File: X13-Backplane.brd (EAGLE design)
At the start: 101.6 x 139.3 mm, 57 parts, among them J1 284512-4, J11 284512-8, J12 284512-8, J2 284512-4, J3 284512-8, J4 284512-8, J5 284512-4, T1 284512-3, T2 284512-3, T3 284512-3, T4 284512-3, T5 284512-3, T6 284512-3, T7 284512-3, T8 284512-3, U1 ULN2003V12, Y1 ECS-80-S-4X

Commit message: draft board layout-  missing power connector
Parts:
- removed C1, C10, C2, C7, C8, C9: 4.7uF, SparkFun-Capacitors:0603
- removed C11: 0.1uF, SparkFun-Capacitors:0603
- removed C3, C4: 100nF, SparkFun-Capacitors:0603
- removed C5: 0.01uF, SparkFun-Capacitors:0603
- removed C6: 1uF, SparkFun-Capacitors:0603
- removed D1, D2, D4: (no value), SparkFun-LED:LED-0603
- removed J11, J12: 284512-8, 284512-8:TE_284512-8
- removed R10, R11: 1k, SparkFun-Resistors:0603
- removed R4, R6: 470, SparkFun-Resistors:0603
- removed R5: 22k, SparkFun-Resistors:0603
- removed R7: (no value), SparkFun-Resistors:0603
- removed R8: 10k, SparkFun-Resistors:0603
- removed R9: 4.7k, SparkFun-Resistors:0603
- removed RESET: (no value), DiscreteComponents:SW_2512
- removed SV1: (no value), con-lsta:FE05-1
- removed U$1, U$2, U$4, U$5, U$6: ESC2BACKPLANE, ESC_to_Backplane_Connectors:ESC2BACKPLANE_WHOLE
- removed U1: ULN2003V12, ULN2003V12:ULN2003V12
- removed Y1: ECS-80-S-4X, ECS-80-S-4X:XTAL_ECS-80-S-4X
- R1: value 1k -> 22k
- R2: value 1k -> 10k
- R3: value 1k -> 4.7k
- U$3: value STM32F042K6T6 -> ESC2BACKPLANE; device PI_Shield_Library:STM32F042K6T6 -> ESC_to_Backplane_Connectors:ESC2BACKPLANE_WHOLE
- U$8: value TCAN337D -> ESC2BACKPLANE; device PI_Shield_Library:TCAN337D -> ESC_to_Backplane_Connectors:ESC2BACKPLANE_WHOLE
- moved J1 329.9 mm to (6.35, 118.1), turned to 90 degrees
- moved T2 243.5 mm to (99.1, 6.35), flipped to the bottom, turned to 180 degrees
- moved T1 233.2 mm to (99.1, 17.8), flipped to the bottom, turned to 180 degrees
- moved MC4 223.3 mm to (99.1, 29.2), flipped to the bottom, turned to 180 degrees
- moved MC3 213.7 mm to (99.1, 40.6), flipped to the bottom, turned to 180 degrees
- moved MC2 204.5 mm to (99.1, 52.1), flipped to the bottom, turned to 180 degrees
- moved MC1 195.8 mm to (99.1, 63.5), flipped to the bottom, turned to 180 degrees
- moved U$7 163.9 mm to (33.0, 96.5), turned to 270 degrees
- moved R3 161.7 mm to (62.2, 36.8), turned to 90 degrees
- moved J4 157.5 mm to (96.5, 86.4), turned to 270 degrees
- moved MUX 149.9 mm to (85.1, 108.0)
- moved R2 139.6 mm to (62.2, 76.2), turned to 90 degrees
- moved J3 129.8 mm to (96.5, 121.9), turned to 270 degrees
- moved U$3 127.0 mm to (33.0, 135.9), turned to 270 degrees
- moved R1 126.4 mm to (62.2, 115.6), turned to 90 degrees
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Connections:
- removed net +3V3: C10.1, U$8.VCC
- removed net ALERT: U$3.PB7
- removed net CAN_RX: U$3.PA11, U$8.RXD
- removed net CAN_TX: U$3.PA12, U$8.TXD
- removed net CLK: U$3.PA9
- removed net DATA: U$3.PA10
- removed net GPIO0: U$3.PA2
- removed net GPIO1: U$3.PB6, U1.4
- removed net GPIO10: U$3.PA5, U1.3
- removed net GPIO11: U$3.PA6, U1.2
- removed net GPIO12: U$3.PA7, U1.1
- removed net GPIO13: U$3.PA8
- removed net GPIO14: U$3.PA1
- removed net GPIO15: U$3.PA0
- removed net GPIO2: U$3.PB4, U1.5
- removed net GPIO3: U$3.PB3, U1.6
- removed net GPIO8: U$3.PA3
- removed net GPIO9: U$3.PA4
- removed net LED: R7.2, U$3.PA15
- removed net N$1: C9.1, R1.1, Y1.2
- removed net N$2: C8.1, R3.1, Y1.1
- removed net N$24: D1.A, R7.1
- removed net N$25: D4.A, R4.1
- removed net N$27: D2.A, R6.1
- removed net N$3: R5.1
- removed net N$5: C11.2, R10.1, R11.2
- removed net OSC_IN: R3.2, U$3.PF0-OSC_IN
- removed net OSC_OUT: R1.2, U$3.PF1-OSC_OUT
- removed net SOL1_1: J12.1, U1.16
- removed net SOL2_1: J12.2, U1.15
- removed net SOL3_1: J12.3, U1.14
- removed net SOL4_1: J12.4, U1.13
- removed net SOL5_1: J12.5, U1.12
- removed net SOL6_1: J12.6, U1.11
- removed net SWCLK: SV1.4
- removed net SWDIO: SV1.2
- net 12V: now also U$3.P$10, U$3.P$11, U$3.P$12, U$3.P$13, U$3.P$9, U$3.P$A, U$3.P$B, U$3.P$C, U$3.P$D, U$3.P$E, U$3.P$O, U$3.P$P, U$3.P$Q, U$3.P$R, U$3.P$S, U$7.P$A, U$7.P$B, U$7.P$C, U$7.P$D, U$7.P$E, U$7.P$O, U$7.P$P, U$7.P$Q, U$7.P$R, U$7.P$S, U$8.P$10, U$8.P$11, U$8.P$12, U$8.P$13, U$8.P$9, U$8.P$A, U$8.P$B, U$8.P$C, U$8.P$D, U$8.P$E, U$8.P$O, U$8.P$P, U$8.P$Q, U$8.P$R, U$8.P$S; no longer J12.7, R4.2, U$1.P$A, U$1.P$B, U$1.P$C, U$1.P$D, U$1.P$E, U$1.P$O, U$1.P$P, U$1.P$Q, U$1.P$R, U$1.P$S, U$2.P$10, U$2.P$11, U$2.P$12, U$2.P$13, U$2.P$23, U$2.P$24, U$2.P$25, U$2.P$26, U$2.P$27, U$2.P$9, U$4.P$A, U$4.P$B, U$4.P$C, U$4.P$D, U$4.P$E, U$4.P$O, U$4.P$P, U$4.P$Q, U$4.P$R, U$4.P$S, U$5.P$10, U$5.P$11, U$5.P$12, U$5.P$13, U$5.P$23, U$5.P$24, U$5.P$25, U$5.P$26, U$5.P$27, U$5.P$9, U$6.P$A, U$6.P$B, U$6.P$C, U$6.P$D, U$6.P$E, U$6.P$O, U$6.P$P, U$6.P$Q, U$6.P$R, U$6.P$S, U$7.P$23, U$7.P$24, U$7.P$25, U$7.P$26, U$7.P$27, U1.9
- net 3.3V: now also U$3.P$G, U$3.P$H, U$3.P$U, U$3.P$V, U$7.P$G, U$7.P$H, U$7.P$U, U$7.P$V, U$8.P$G, U$8.P$H, U$8.P$U, U$8.P$V; no longer C1.1, C2.1, C3.1, C4.1, C5.1, C6.1, J11.5, R2.2, R6.2, SV1.5, U$1.P$G, U$1.P$H, U$1.P$U, U$1.P$V, U$3.VDD, U$3.VDDA, U$3.VDDIO2, U$4.P$G, U$4.P$H, U$4.P$U, U$4.P$V, U$6.P$G, U$6.P$H, U$6.P$U, U$6.P$V
- net CAN_H: now also U$3.P$6, U$8.P$6; no longer R10.2, U$2.P$6, U$5.P$6, U$8.CANH
- net CAN_L: now also U$3.P$7, U$8.P$7; no longer R11.1, U$2.P$7, U$5.P$7, U$8.CANL
- net ESC-ID_1: now also R1.2, U$3.P$8; no longer R5.2, U$7.P$8
- net ESC-ID_2: now also R2.2, U$7.P$8; no longer R8.2, U$5.P$8
- net ESC-ID_3: now also R3.2, U$8.P$8; no longer R9.2, U$2.P$8
- net GND: now also R1.1, R2.1, R3.1, U$3.P$1, U$3.P$15, U$3.P$16, U$3.P$17, U$3.P$18, U$3.P$2, U$3.P$23, U$3.P$24, U$3.P$25, U$3.P$26, U$3.P$27, U$3.P$3, U$3.P$4, U$3.P$AA, U$3.P$BB, U$3.P$J, U$3.P$K, U$3.P$L, U$3.P$M, U$3.P$N, U$3.P$X, U$3.P$Y, U$3.P$Z, U$7.P$23, U$7.P$24, U$7.P$25, U$7.P$26, U$7.P$27, U$7.P$AA, U$7.P$BB, U$7.P$J, U$7.P$K, U$7.P$L, U$7.P$M, U$7.P$N, U$7.P$X, U$7.P$Y, U$7.P$Z, U$8.P$1, U$8.P$15, U$8.P$16, U$8.P$17, U$8.P$18, U$8.P$2, U$8.P$23, U$8.P$24, U$8.P$25, U$8.P$26, U$8.P$27, U$8.P$3, U$8.P$4, U$8.P$AA, U$8.P$BB, U$8.P$J, U$8.P$K, U$8.P$L, U$8.P$M, U$8.P$N, U$8.P$X, U$8.P$Y, U$8.P$Z; no longer C1.2, C10.2, C11.1, C2.2, C3.2, C4.2, C5.2, C6.2, C7.2, C8.2, C9.2, D1.C, D2.C, D4.C, J11.1, R8.1, R9.1, RESET.1, SV1.3, U$1.P$AA, U$1.P$BB, U$1.P$J, U$1.P$K, U$1.P$L, U$1.P$M, U$1.P$N, U$1.P$X, U$1.P$Y, U$1.P$Z, U$2.P$1, U$2.P$15, U$2.P$16, U$2.P$17, U$2.P$18, U$2.P$2, U$2.P$3, U$2.P$4, U$3.PB8-BOOT0, U$3.VSS, U$3.VSS1, U$4.P$AA, U$4.P$BB, U$4.P$J, U$4.P$K, U$4.P$L, U$4.P$M, U$4.P$N, U$4.P$X, U$4.P$Y, U$4.P$Z, U$5.P$1, U$5.P$15, U$5.P$16, U$5.P$17, U$5.P$18, U$5.P$2, U$5.P$3, U$5.P$4, U$6.P$AA, U$6.P$BB, U$6.P$J, U$6.P$K, U$6.P$L, U$6.P$M, U$6.P$N, U$6.P$X, U$6.P$Y, U$6.P$Z, U$8.GND, U1.8
- net NRST: now also U$3.P$20, U$8.P$20; no longer C7.1, J11.6, R2.1, RESET.2, SV1.1, U$2.P$20, U$3.NRST, U$5.P$20
- net PROG_1: now also U$3.P$5; no longer J11.2, U$7.P$5
- net PROG_2: now also U$7.P$5; no longer J11.3, U$5.P$5
- net PROG_3: now also U$8.P$5; no longer J11.4, U$2.P$5
- net SWCLK_1: now also U$3.P$22; no longer U$7.P$22
- net SWCLK_2: now also U$7.P$22; no longer U$5.P$22
- net SWCLK_3: now also U$8.P$22; no longer U$2.P$22
- net SWCLK_4: no longer U$3.PA14
- net SWCLK_IN: no longer J11.7
- net SWDIO_1: now also U$3.P$21; no longer U$7.P$21
- net SWDIO_2: now also U$7.P$21; no longer U$5.P$21
- net SWDIO_3: now also U$8.P$21; no longer U$2.P$21
- net SWDIO_4: no longer U$3.PA13
- net SWDIO_IN: no longer J11.8, J12.8

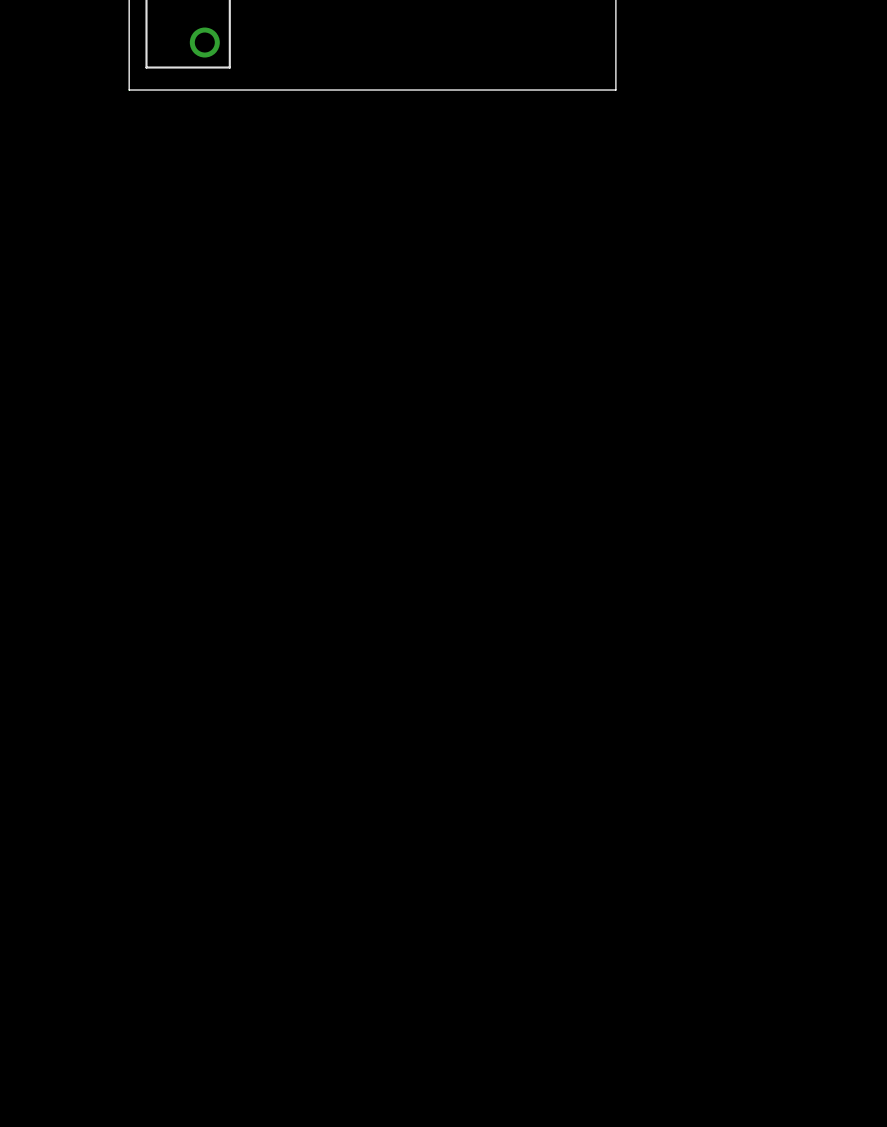
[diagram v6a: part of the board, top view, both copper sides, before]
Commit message: added back solenoid board
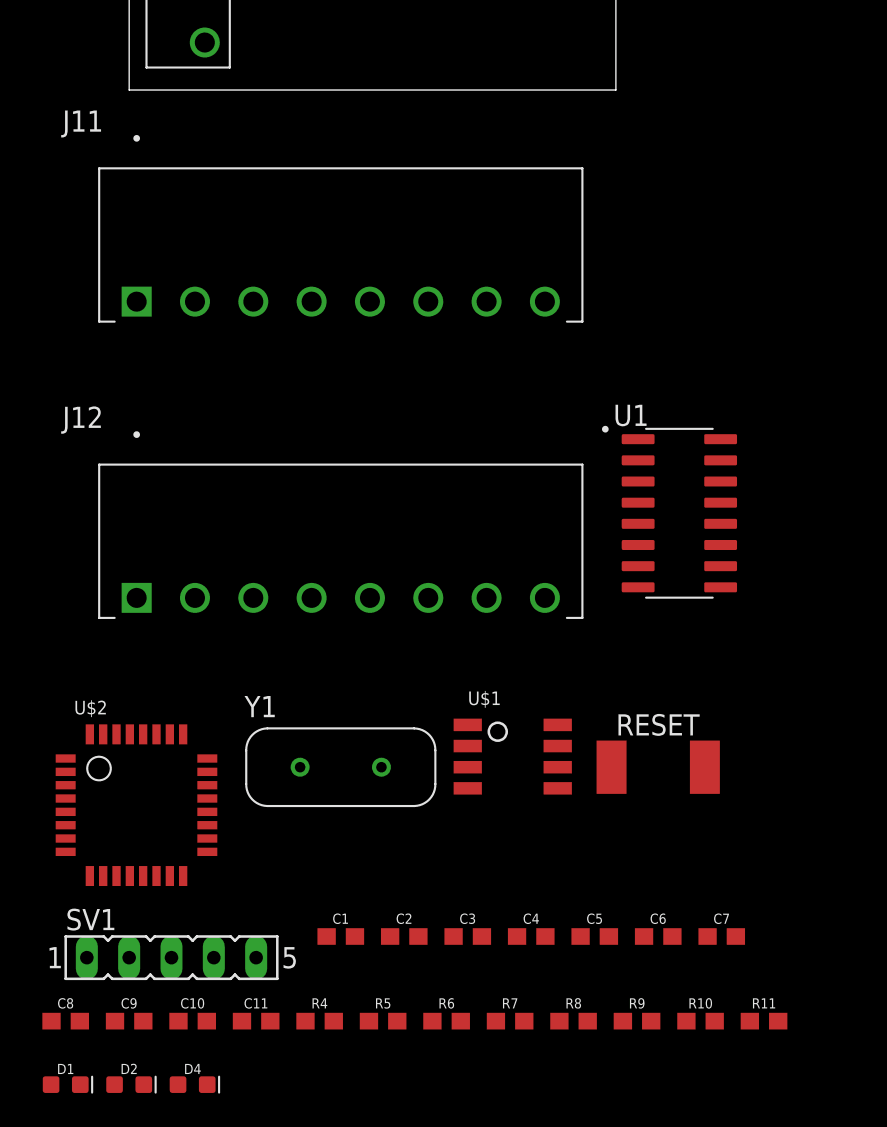
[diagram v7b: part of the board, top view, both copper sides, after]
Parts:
- added C1, C10, C2, C7, C8, C9: 4.7uF, SparkFun-Capacitors:0603
- added C11: 0.1uF, SparkFun-Capacitors:0603
- added C3, C4: 100nF, SparkFun-Capacitors:0603
- added C5: 0.01uF, SparkFun-Capacitors:0603
- added C6: 1uF, SparkFun-Capacitors:0603
- added D1, D2, D4: (no value), SparkFun-LED:LED-0603
- added J11, J12: 284512-8, 284512-8:TE_284512-8
- added R10, R11, R5, R7, R8: 1k, SparkFun-Resistors:0603
- added R4, R6: 470, SparkFun-Resistors:0603
- added R9: (no value), SparkFun-Resistors:0603
- added RESET: (no value), DiscreteComponents:SW_2512
- added SV1: (no value), con-lsta:FE05-1
- added U$1: TCAN337D, PI_Shield_Library:TCAN337D
- added U$2: STM32F042K6T6, PI_Shield_Library:STM32F042K6T6
- added U1: ULN2003V12, ULN2003V12:ULN2003V12
- added Y1: ECS-80-S-4X, ECS-80-S-4X:XTAL_ECS-80-S-4X
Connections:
- new net +3V3: C10.1, U$1.VCC
- new net ALERT1: U$2.PB7
- new net ALERT2: U$2.PB5
- new net C2_1: U$2.PB0
- new net C2_2: U$2.PB1
- new net CAN_RX: U$1.RXD, U$2.PA11
- new net CAN_TX: U$1.TXD, U$2.PA12
- new net CLK: U$2.PA9
- new net DATA: U$2.PA10
- new net GPIO0: U$2.PA2
- new net GPIO1: U$2.PB6, U1.4
- new net GPIO10: U$2.PA5, U1.3
- new net GPIO11: U$2.PA6, U1.2
- new net GPIO12: U$2.PA7, U1.1
- new net GPIO13: U$2.PA8
- new net GPIO14: U$2.PA1
- new net GPIO15: U$2.PA0
- new net GPIO2: U$2.PB4, U1.5
- new net GPIO3: U$2.PB3, U1.6
- new net GPIO8: U$2.PA3
- new net GPIO9: U$2.PA4
- new net LED: R9.2, U$2.PA15
- new net N$1: C9.1, R5.1, Y1.2
- new net N$2: C8.1, R8.1, Y1.1
- new net N$24: D1.A, R9.1
- new net N$25: D4.A, R4.1
- new net N$27: D2.A, R6.1
- new net N$5: C11.2, R10.1, R11.2
- new net OSC_IN: R8.2, U$2.PF0-OSC_IN
- new net OSC_OUT: R5.2, U$2.PF1-OSC_OUT
- new net PROG_4: J11.2
- new net SOL1_1: J12.1, U1.16
- new net SOL2_1: J12.2, U1.15
- new net SOL3_1: J12.3, U1.14
- new net SOL4_1: J12.4, U1.13
- new net SOL5_1: J12.5, U1.12
- new net SOL6_1: J12.6, U1.11
- new net SWCLK: SV1.4
- new net SWDIO: SV1.2
- net 12V: now also J12.7, R4.2, U$3.P$23, U$3.P$24, U$3.P$25, U$3.P$26, U$3.P$27, U$7.P$23, U$7.P$24, U$7.P$25, U$7.P$26, U$7.P$27, U$8.P$23, U$8.P$24, U$8.P$25, U$8.P$26, U$8.P$27, U1.9
- net 3.3V: now also C1.1, C2.1, C3.1, C4.1, C5.1, C6.1, J11.5, R6.2, R7.2, SV1.5, U$2.VDD, U$2.VDDA, U$2.VDDIO2
- net CAN_H: now also R10.2, U$1.CANH
- net CAN_L: now also R11.1, U$1.CANL
- net GND: now also C1.2, C10.2, C11.1, C2.2, C3.2, C4.2, C5.2, C6.2, C7.2, C8.2, C9.2, D1.C, D2.C, D4.C, J11.1, RESET.1, SV1.3, U$1.GND, U$2.PB8-BOOT0, U$2.VSS, U$2.VSS1, U1.8; no longer U$3.P$23, U$3.P$24, U$3.P$25, U$3.P$26, U$3.P$27, U$7.P$23, U$7.P$24, U$7.P$25, U$7.P$26, U$7.P$27, U$8.P$23, U$8.P$24, U$8.P$25, U$8.P$26, U$8.P$27
- net NRST: now also C7.1, J11.6, R7.1, RESET.2, SV1.1, U$2.NRST
- net PROG_2: now also J11.3
- net PROG_3: now also J11.4
- net SWCLK_4: now also U$2.PA14
- net SWCLK_IN: now also J11.7
- net SWDIO_4: now also U$2.PA13
- net SWDIO_IN: now also J11.8, J12.8

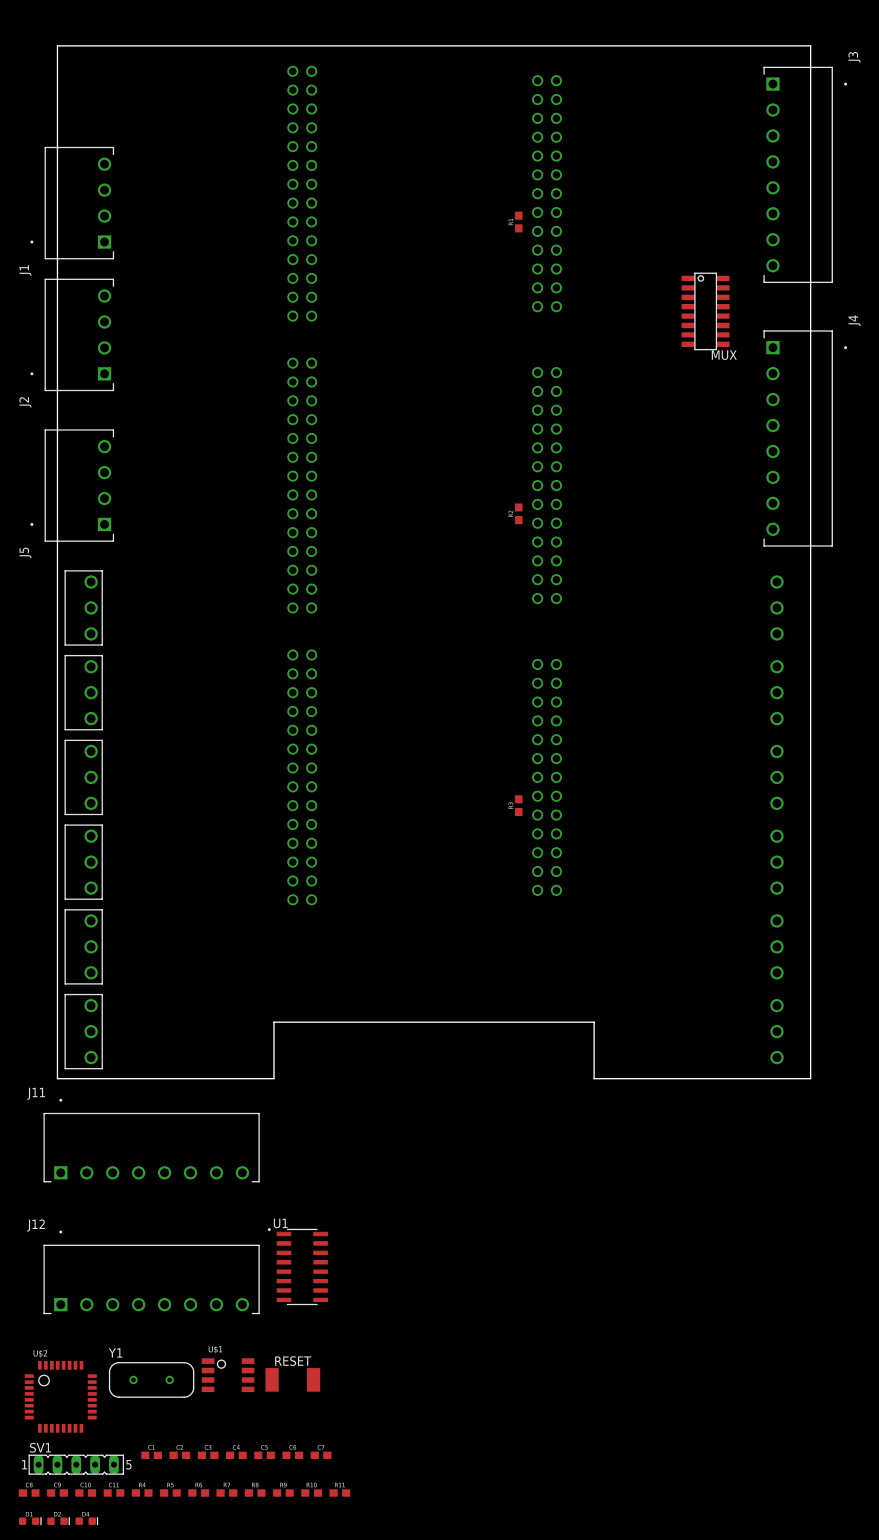
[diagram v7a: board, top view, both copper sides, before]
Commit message: removed solenoid board
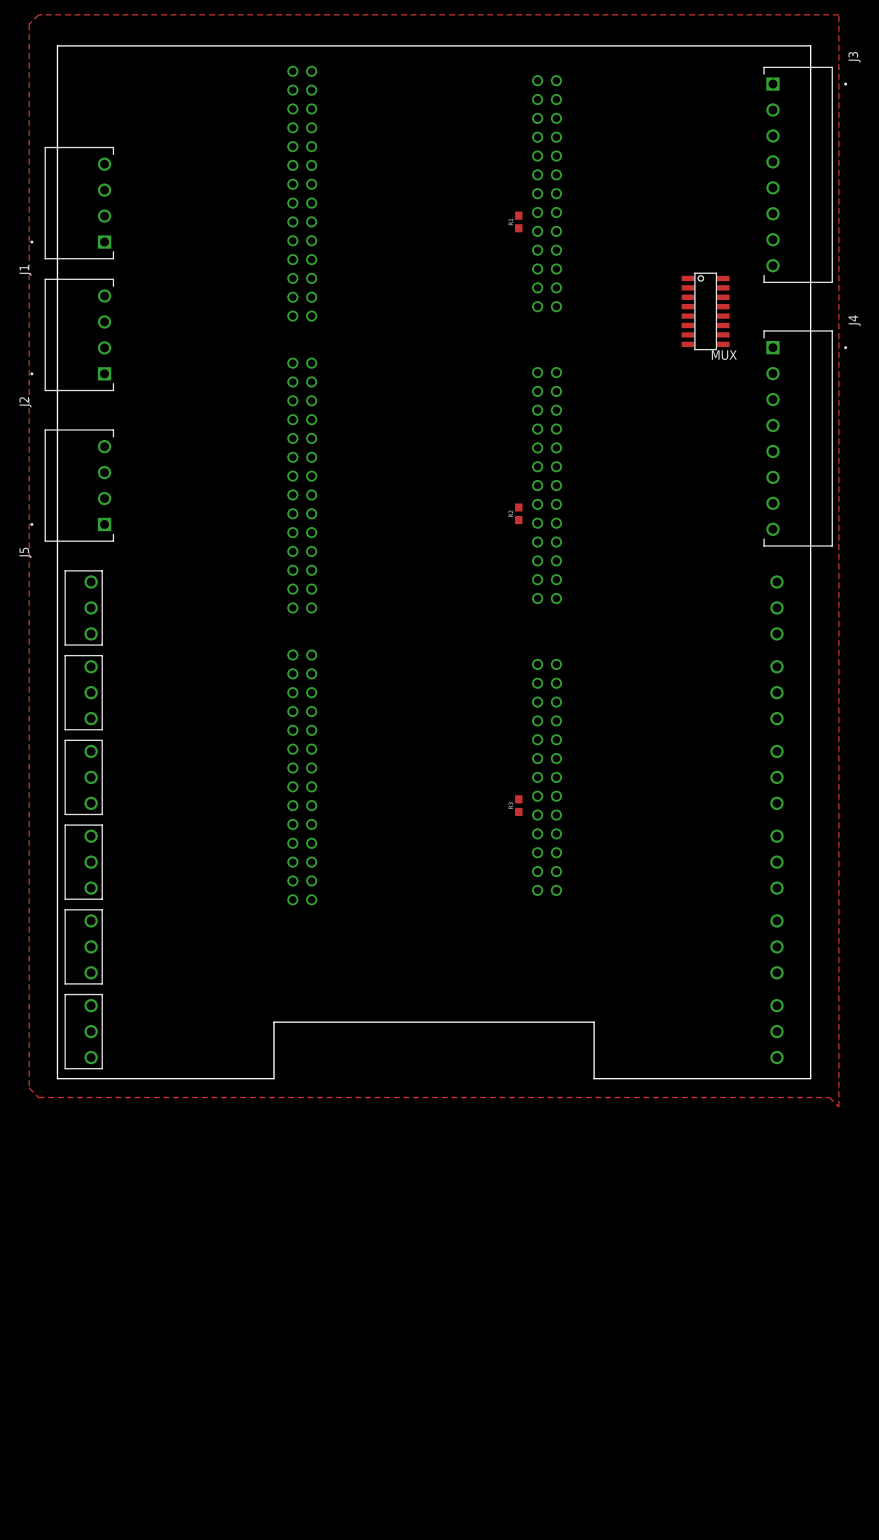
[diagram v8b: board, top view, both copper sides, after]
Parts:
- removed C1, C10, C2, C7, C8, C9: 4.7uF, SparkFun-Capacitors:0603
- removed C11: 0.1uF, SparkFun-Capacitors:0603
- removed C3, C4: 100nF, SparkFun-Capacitors:0603
- removed C5: 0.01uF, SparkFun-Capacitors:0603
- removed C6: 1uF, SparkFun-Capacitors:0603
- removed D1, D2, D4: (no value), SparkFun-LED:LED-0603
- removed J11, J12: 284512-8, 284512-8:TE_284512-8
- removed R10, R11, R5, R7, R8: 1k, SparkFun-Resistors:0603
- removed R4, R6: 470, SparkFun-Resistors:0603
- removed R9: (no value), SparkFun-Resistors:0603
- removed RESET: (no value), DiscreteComponents:SW_2512
- removed SV1: (no value), con-lsta:FE05-1
- removed U$1: TCAN337D, PI_Shield_Library:TCAN337D
- removed U$2: STM32F042K6T6, PI_Shield_Library:STM32F042K6T6
- removed U1: ULN2003V12, ULN2003V12:ULN2003V12
- removed Y1: ECS-80-S-4X, ECS-80-S-4X:XTAL_ECS-80-S-4X
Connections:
- removed net +3V3: C10.1, U$1.VCC
- removed net ALERT1: U$2.PB7
- removed net ALERT2: U$2.PB5
- removed net C2_1: U$2.PB0
- removed net C2_2: U$2.PB1
- removed net CAN_RX: U$1.RXD, U$2.PA11
- removed net CAN_TX: U$1.TXD, U$2.PA12
- removed net CLK: U$2.PA9
- removed net DATA: U$2.PA10
- removed net GPIO0: U$2.PA2
- removed net GPIO1: U$2.PB6, U1.4
- removed net GPIO10: U$2.PA5, U1.3
- removed net GPIO11: U$2.PA6, U1.2
- removed net GPIO12: U$2.PA7, U1.1
- removed net GPIO13: U$2.PA8
- removed net GPIO14: U$2.PA1
- removed net GPIO15: U$2.PA0
- removed net GPIO2: U$2.PB4, U1.5
- removed net GPIO3: U$2.PB3, U1.6
- removed net GPIO8: U$2.PA3
- removed net GPIO9: U$2.PA4
- removed net LED: R9.2, U$2.PA15
- removed net N$1: C9.1, R5.1, Y1.2
- removed net N$2: C8.1, R8.1, Y1.1
- removed net N$24: D1.A, R9.1
- removed net N$25: D4.A, R4.1
- removed net N$27: D2.A, R6.1
- removed net N$5: C11.2, R10.1, R11.2
- removed net OSC_IN: R8.2, U$2.PF0-OSC_IN
- removed net OSC_OUT: R5.2, U$2.PF1-OSC_OUT
- removed net PROG_4: J11.2
- removed net SOL1_1: J12.1, U1.16
- removed net SOL2_1: J12.2, U1.15
- removed net SOL3_1: J12.3, U1.14
- removed net SOL4_1: J12.4, U1.13
- removed net SOL5_1: J12.5, U1.12
- removed net SOL6_1: J12.6, U1.11
- removed net SWCLK: SV1.4
- removed net SWDIO: SV1.2
- net 12V: no longer J12.7, R4.2, U1.9
- net 3.3V: no longer C1.1, C2.1, C3.1, C4.1, C5.1, C6.1, J11.5, R6.2, R7.2, SV1.5, U$2.VDD, U$2.VDDA, U$2.VDDIO2
- net CAN_H: no longer R10.2, U$1.CANH
- net CAN_L: no longer R11.1, U$1.CANL
- net GND: no longer C1.2, C10.2, C11.1, C2.2, C3.2, C4.2, C5.2, C6.2, C7.2, C8.2, C9.2, D1.C, D2.C, D4.C, J11.1, RESET.1, SV1.3, U$1.GND, U$2.PB8-BOOT0, U$2.VSS, U$2.VSS1, U1.8
- net NRST: no longer C7.1, J11.6, R7.1, RESET.2, SV1.1, U$2.NRST
- net PROG_2: no longer J11.3
- net PROG_3: no longer J11.4
- net SWCLK_4: no longer U$2.PA14
- net SWCLK_IN: no longer J11.7
- net SWDIO_4: no longer U$2.PA13
- net SWDIO_IN: no longer J11.8, J12.8
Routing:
- added copper zone on layer 1, net GND
